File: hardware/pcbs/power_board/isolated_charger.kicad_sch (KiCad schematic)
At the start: 12 parts

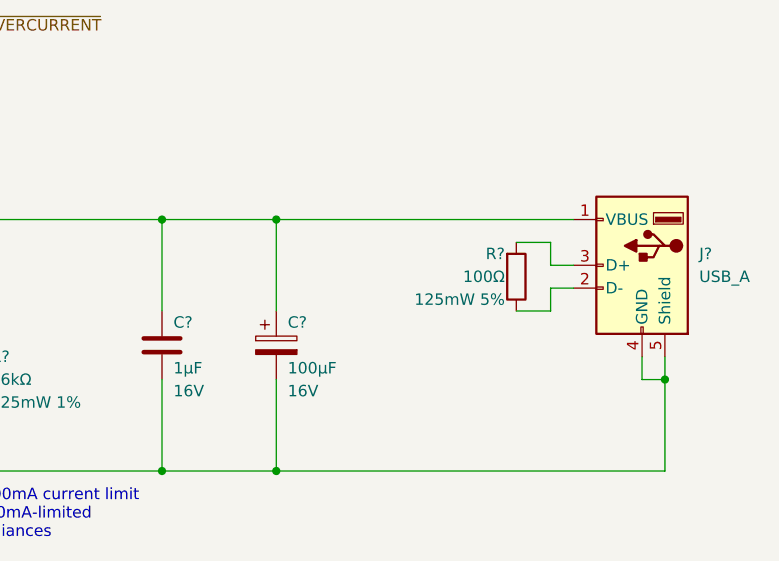
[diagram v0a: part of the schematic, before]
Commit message: power_board: schematic for fan controller
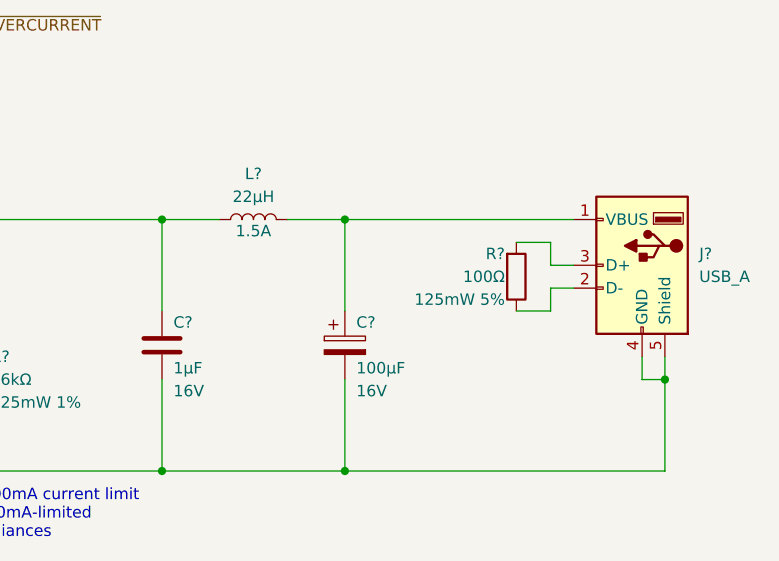
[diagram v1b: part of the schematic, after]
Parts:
- added L?: 22μH, Inductor_SMD:L_Sunlord_SWPA6045S, symbol Device:L
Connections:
- net at C?.1, U?.6 (OUT): now also L?.1; no longer C?.1, J?.1 (VBUS)
- new net: C?.1, J?.1 (VBUS), L?.2
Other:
- moved on the sheet: C?
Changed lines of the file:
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@@
   (junction (at 201.93 88.9) (diameter 0) (color 0 0 0 0)
   )
-  (junction (at 214.63 116.84) (diameter 0) (color 0 0 0 0)
-  )
   (junction (at 132.08 88.9) (diameter 0) (color 0 0 0 0)
   )
+  (junction (at 222.25 88.9) (diameter 0) (color 0 0 0 0)
+  )
   (junction (at 201.93 116.84) (diameter 0) (color 0 0 0 0)
   )
@@
   (junction (at 257.81 106.68) (diameter 0) (color 0 0 0 0)
   )
+  (junction (at 222.25 116.84) (diameter 0) (color 0 0 0 0)
+  )
   (junction (at 167.64 116.84) (diameter 0) (color 0 0 0 0)
   )
-  (junction (at 214.63 88.9) (diameter 0) (color 0 0 0 0)
-  )
   (junction (at 67.31 88.9) (diameter 0) (color 0 0 0 0)
   )
@@
     (stroke (width 0) (type default))
   )
-  (wire (pts (xy 201.93 116.84) (xy 214.63 116.84))
+  (wire (pts (xy 201.93 116.84) (xy 222.25 116.84))
     (stroke (width 0) (type default))
   )
@@
     (stroke (width 0) (type default))
   )
-  (wire (pts (xy 201.93 88.9) (xy 214.63 88.9))
+  (wire (pts (xy 201.93 88.9) (xy 208.28 88.9))
     (stroke (width 0) (type default))
   )
@@
     (stroke (width 0) (type default))
   )
+  (wire (pts (xy 222.25 116.84) (xy 257.81 116.84))
+    (stroke (width 0) (type default))
+  )
   (wire (pts (xy 138.43 52.07) (xy 152.4 52.07))
     (stroke (width 0) (type default))
@@
     (stroke (width 0) (type default))
   )
-  (wire (pts (xy 214.63 116.84) (xy 257.81 116.84))
-    (stroke (width 0) (type default))
-  )
   (wire (pts (xy 171.45 67.31) (xy 180.34 67.31))
     (stroke (width 0) (type default))
@@
     (stroke (width 0) (type default))
   )
-  (wire (pts (xy 214.63 88.9) (xy 247.65 88.9))
-    (stroke (width 0) (type default))
-  )
   (wire (pts (xy 132.08 88.9) (xy 132.08 99.06))
     (stroke (width 0) (type default))
@@
     (stroke (width 0) (type default))
   )
-  (wire (pts (xy 214.63 88.9) (xy 214.63 99.06))
+  (wire (pts (xy 222.25 88.9) (xy 222.25 99.06))
     (stroke (width 0) (type default))
   )
@@
     (stroke (width 0) (type default))
   )
+  (wire (pts (xy 222.25 88.9) (xy 247.65 88.9))
+    (stroke (width 0) (type default))
+  )
   (wire (pts (xy 132.08 88.9) (xy 138.43 88.9))
     (stroke (width 0) (type default))
@@
     (stroke (width 0) (type default))
   )
-  (wire (pts (xy 214.63 106.68) (xy 214.63 116.84))
+  (wire (pts (xy 222.25 106.68) (xy 222.25 116.84))
     (stroke (width 0) (type default))
   )
@@
   )
   (wire (pts (xy 152.4 62.23) (xy 152.4 67.31))
+    (stroke (width 0) (type default))
+  )
+  (wire (pts (xy 215.9 88.9) (xy 222.25 88.9))
     (stroke (width 0) (type default))
   )
@@
         (path "/4b166175-80a4-48c6-994d-6e62a6160b87/2e2b9578-5dbd-4b2d-88fb-256ac9c8dd75/bdb69c9c-123a-4faa-b5c1-7130aac5ebc2"
           (reference "C?") (unit 1)
+        )
+      )
+    )
+  )
+  (symbol (lib_id "Device:L") (at 212.09 88.9 90) (unit 1)
+    (in_bom yes) (on_board yes) (dnp no)
+    (property "Reference" "L?" (at 212.09 83.82 90)
+      (effects (font (size 1.27 1.27)))
+    )
+    (property "Value" "22μH" (at 212.09 86.36 90)
+      (effects (font (size 1.27 1.27)))
+    )
+    (property "Footprint" "Inductor_SMD:L_Sunlord_SWPA6045S" (at 212.09 88.9 0)
+      (effects (font (size 1.27 1.27)) hide)
+    )
+    (property "Datasheet" "~" (at 212.09 88.9 0)
+      (effects (font (size 1.27 1.27)) hide)
+    )
+    (property "Shop" "https://store.comet.bg/Catalogue/Product/49991/" (at 212.09 88.9 90)
+      (effects (font (size 1.27 1.27)) hide)
+    )
+    (property "Info" "1.5A" (at 212.09 90.17 90)
+      (effects (font (size 1.27 1.27)))
+    )
+    (pin "1")
+    (pin "2")
+    (instances
+      (project "power_board"
+        (path "/4b166175-80a4-48c6-994d-6e62a6160b87/2e2b9578-5dbd-4b2d-88fb-256ac9c8dd75/32f9baea-32bc-4a84-b83a-18c67cc6248e"
+          (reference "L?") (unit 1)
+        )
+        (path "/4b166175-80a4-48c6-994d-6e62a6160b87/2e2b9578-5dbd-4b2d-88fb-256ac9c8dd75/5f362cd5-d351-4250-994a-9f336837035c"
+          (reference "L?") (unit 1)
+        )
+        (path "/4b166175-80a4-48c6-994d-6e62a6160b87/2e2b9578-5dbd-4b2d-88fb-256ac9c8dd75/6373063e-1125-40d9-b0ec-3e2cb2886aea"
+          (reference "L?") (unit 1)
+        )
+        (path "/4b166175-80a4-48c6-994d-6e62a6160b87/2e2b9578-5dbd-4b2d-88fb-256ac9c8dd75/bdb69c9c-123a-4faa-b5c1-7130aac5ebc2"
+          (reference "L?") (unit 1)
         )
       )
@@
     )
   )
-  (symbol (lib_id "Device:C_Polarized") (at 214.63 102.87 0) (unit 1)
+  (symbol (lib_id "Device:C_Polarized") (at 222.25 102.87 0) (unit 1)
     (in_bom yes) (on_board yes) (dnp no)
-    (property "Reference" "C?" (at 215.9 100.33 0)
-      (effects (font (size 1.27 1.27)) (justify left))
-    )
-    (property "Value" "100μF" (at 215.9 105.41 0)
-      (effects (font (size 1.27 1.27)) (justify left))
-    )
-    (property "Footprint" "Capacitor_SMD:CP_Elec_6.3x5.4" (at 215.5952 106.68 0)
-      (effects (font (size 1.27 1.27)) hide)
-    )
-    (property "Datasheet" "~" (at 214.63 102.87 0)
-      (effects (font (size 1.27 1.27)) hide)
-    )
-    (property "Shop" "https://store.comet.bg/Catalogue/Product/29563/" (at 214.63 102.87 0)
-      (effects (font (size 1.27 1.27)) hide)
-    )
-    (property "Info" "16V" (at 215.9 107.95 0)
-      (effects (font (size 1.27 1.27)) (justify left))
-    )
+    (property "Reference" "C?" (at 223.52 100.33 0)
+      (effects (font (size 1.27 1.27)) (justify left))
+    )
+    (property "Value" "100μF" (at 223.52 105.41 0)
+      (effects (font (size 1.27 1.27)) (justify left))
+    )
+    (property "Footprint" "Capacitor_SMD:CP_Elec_6.3x5.4" (at 223.2152 106.68 0)
+      (effects (font (size 1.27 1.27)) hide)
+    )
+    (property "Datasheet" "~" (at 222.25 102.87 0)
+      (effects (font (size 1.27 1.27)) hide)
+    )
+    (property "Shop" "https://store.comet.bg/Catalogue/Product/29563/" (at 222.25 102.87 0)
+      (effects (font (size 1.27 1.27)) hide)
+    )
+    (property "Info" "16V" (at 223.52 107.95 0)
+      (effects (font (size 1.27 1.27)) (justify left))
+    )

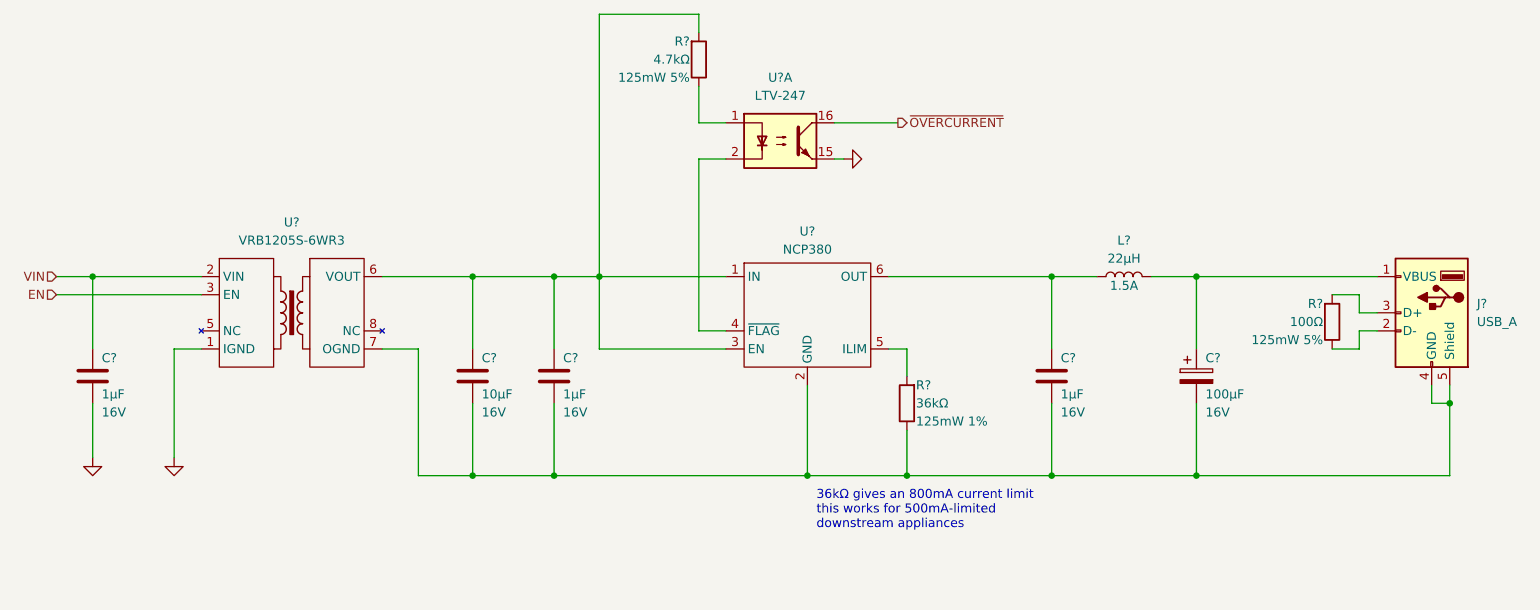
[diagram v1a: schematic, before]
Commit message: power_board: add temperature sensor and GPIOs to schematic
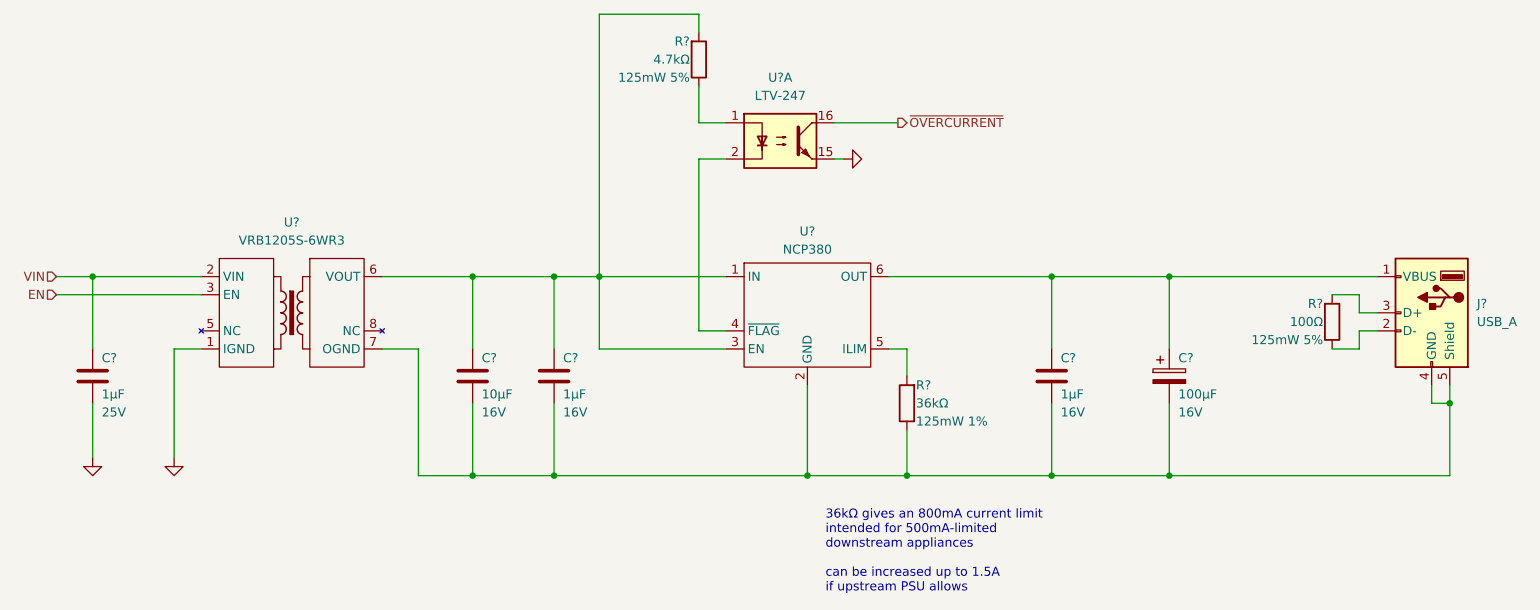
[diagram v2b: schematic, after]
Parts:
- removed L?: 22μH, Inductor_SMD:L_Sunlord_SWPA6045S, symbol Device:L
- C?: Info 16V -> 25V; Shop https://store.comet.bg/Catalogue/Product/16789/ -> https://store.comet.bg/Catalogue/Product/9031/
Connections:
- net at C?.1, U?.6 (OUT): now also C?.1, J?.1 (VBUS)
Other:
- note added: "36kΩ gives an 800mA current limit intended for 500mA-limited downstream appliances can be increased up to 1.5A if upstream PSU allows"
- note removed: "36kΩ gives an 800mA current limit this works for 500mA-limited downstream appliances"
- moved on the sheet: C?
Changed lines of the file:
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@@
   (junction (at 132.08 88.9) (diameter 0) (color 0 0 0 0)
   )
-  (junction (at 222.25 88.9) (diameter 0) (color 0 0 0 0)
-  )
   (junction (at 201.93 116.84) (diameter 0) (color 0 0 0 0)
   )
@@
   (junction (at 257.81 106.68) (diameter 0) (color 0 0 0 0)
   )
-  (junction (at 222.25 116.84) (diameter 0) (color 0 0 0 0)
+  (junction (at 218.44 116.84) (diameter 0) (color 0 0 0 0)
   )
   (junction (at 167.64 116.84) (diameter 0) (color 0 0 0 0)
@@
   (junction (at 67.31 88.9) (diameter 0) (color 0 0 0 0)
   )
+  (junction (at 218.44 88.9) (diameter 0) (color 0 0 0 0)
+  )
   (junction (at 181.61 116.84) (diameter 0) (color 0 0 0 0)
   )
@@
     (stroke (width 0) (type default))
   )
-  (wire (pts (xy 201.93 116.84) (xy 222.25 116.84))
+  (wire (pts (xy 201.93 116.84) (xy 218.44 116.84))
     (stroke (width 0) (type default))
   )
@@
     (stroke (width 0) (type default))
   )
-  (wire (pts (xy 201.93 88.9) (xy 208.28 88.9))
+  (wire (pts (xy 201.93 88.9) (xy 218.44 88.9))
     (stroke (width 0) (type default))
   )
@@
     (stroke (width 0) (type default))
   )
-  (wire (pts (xy 222.25 116.84) (xy 257.81 116.84))
-    (stroke (width 0) (type default))
-  )
   (wire (pts (xy 138.43 52.07) (xy 152.4 52.07))
     (stroke (width 0) (type default))
@@
     (stroke (width 0) (type default))
   )
-  (wire (pts (xy 222.25 88.9) (xy 222.25 99.06))
+  (wire (pts (xy 218.44 88.9) (xy 218.44 99.06))
     (stroke (width 0) (type default))
   )
@@
     (stroke (width 0) (type default))
   )
-  (wire (pts (xy 222.25 88.9) (xy 247.65 88.9))
+  (wire (pts (xy 218.44 88.9) (xy 247.65 88.9))
     (stroke (width 0) (type default))
   )
@@
     (stroke (width 0) (type default))
   )
+  (wire (pts (xy 218.44 116.84) (xy 257.81 116.84))
+    (stroke (width 0) (type default))
+  )
   (wire (pts (xy 67.31 106.68) (xy 67.31 114.3))
     (stroke (width 0) (type default))
@@
     (stroke (width 0) (type default))
   )
-  (wire (pts (xy 222.25 106.68) (xy 222.25 116.84))
+  (wire (pts (xy 218.44 106.68) (xy 218.44 116.84))
     (stroke (width 0) (type default))
   )
@@
     (stroke (width 0) (type default))
   )
-  (wire (pts (xy 215.9 88.9) (xy 222.25 88.9))
-    (stroke (width 0) (type default))
-  )
   (wire (pts (xy 152.4 96.52) (xy 152.4 72.39))
     (stroke (width 0) (type default))
@@
     (stroke (width 0) (type default))
   )
-  (text "36kΩ gives an 800mA current limit\nthis works for 500mA-limited\ndownstream appliances"
-    (at 168.91 124.46 0)
+  (text "36kΩ gives an 800mA current limit\nintended for 500mA-limited\ndownstream appliances\n\ncan be increased up to 1.5A\nif upstream PSU allows"
+    (at 170.18 133.35 0)
     (effects (font (size 1.27 1.27)) (justify left bottom))
   )
@@
       (effects (font (size 1.27 1.27)) hide)
     )
-    (property "Info" "16V" (at 68.58 107.95 0)
-      (effects (font (size 1.27 1.27)) (justify left))
-    )
-    (property "Shop" "https://store.comet.bg/Catalogue/Product/16789/" (at 67.31 102.87 0)
+    (property "Info" "25V" (at 68.58 107.95 0)
+      (effects (font (size 1.27 1.27)) (justify left))
+    )
+    (property "Shop" "https://store.comet.bg/Catalogue/Product/9031/" (at 67.31 102.87 0)
       (effects (font (size 1.27 1.27)) hide)
     )
@@
         (path "/4b166175-80a4-48c6-994d-6e62a6160b87/2e2b9578-5dbd-4b2d-88fb-256ac9c8dd75/bdb69c9c-123a-4faa-b5c1-7130aac5ebc2"
           (reference "C?") (unit 1)
-        )
-      )
-    )
-  )
-  (symbol (lib_id "Device:L") (at 212.09 88.9 90) (unit 1)
-    (in_bom yes) (on_board yes) (dnp no)
-    (property "Reference" "L?" (at 212.09 83.82 90)
-      (effects (font (size 1.27 1.27)))
-    )
-    (property "Value" "22μH" (at 212.09 86.36 90)
-      (effects (font (size 1.27 1.27)))
-    )
-    (property "Footprint" "Inductor_SMD:L_Sunlord_SWPA6045S" (at 212.09 88.9 0)
-      (effects (font (size 1.27 1.27)) hide)
-    )
-    (property "Datasheet" "~" (at 212.09 88.9 0)
-      (effects (font (size 1.27 1.27)) hide)
-    )
-    (property "Shop" "https://store.comet.bg/Catalogue/Product/49991/" (at 212.09 88.9 90)
-      (effects (font (size 1.27 1.27)) hide)
-    )
-    (property "Info" "1.5A" (at 212.09 90.17 90)
-      (effects (font (size 1.27 1.27)))
-    )
-    (pin "1")
-    (pin "2")
-    (instances
-      (project "power_board"
-        (path "/4b166175-80a4-48c6-994d-6e62a6160b87/2e2b9578-5dbd-4b2d-88fb-256ac9c8dd75/32f9baea-32bc-4a84-b83a-18c67cc6248e"
-          (reference "L?") (unit 1)
-        )
-        (path "/4b166175-80a4-48c6-994d-6e62a6160b87/2e2b9578-5dbd-4b2d-88fb-256ac9c8dd75/5f362cd5-d351-4250-994a-9f336837035c"
-          (reference "L?") (unit 1)
-        )
-        (path "/4b166175-80a4-48c6-994d-6e62a6160b87/2e2b9578-5dbd-4b2d-88fb-256ac9c8dd75/6373063e-1125-40d9-b0ec-3e2cb2886aea"
-          (reference "L?") (unit 1)
-        )
-        (path "/4b166175-80a4-48c6-994d-6e62a6160b87/2e2b9578-5dbd-4b2d-88fb-256ac9c8dd75/bdb69c9c-123a-4faa-b5c1-7130aac5ebc2"
-          (reference "L?") (unit 1)
         )
       )
@@
     )
   )
-  (symbol (lib_id "Device:C_Polarized") (at 222.25 102.87 0) (unit 1)
+  (symbol (lib_id "Device:C_Polarized") (at 218.44 102.87 0) (unit 1)
     (in_bom yes) (on_board yes) (dnp no)
-    (property "Reference" "C?" (at 223.52 100.33 0)
-      (effects (font (size 1.27 1.27)) (justify left))
-    )
-    (property "Value" "100μF" (at 223.52 105.41 0)
-      (effects (font (size 1.27 1.27)) (justify left))
-    )
-    (property "Footprint" "Capacitor_SMD:CP_Elec_6.3x5.4" (at 223.2152 106.68 0)
-      (effects (font (size 1.27 1.27)) hide)
-    )
-    (property "Datasheet" "~" (at 222.25 102.87 0)
-      (effects (font (size 1.27 1.27)) hide)
-    )
-    (property "Shop" "https://store.comet.bg/Catalogue/Product/29563/" (at 222.25 102.87 0)
-      (effects (font (size 1.27 1.27)) hide)
-    )
-    (property "Info" "16V" (at 223.52 107.95 0)
-      (effects (font (size 1.27 1.27)) (justify left))
-    )
+    (property "Reference" "C?" (at 219.71 100.33 0)
+      (effects (font (size 1.27 1.27)) (justify left))
+    )
+    (property "Value" "100μF" (at 219.71 105.41 0)
+      (effects (font (size 1.27 1.27)) (justify left))
+    )
+    (property "Footprint" "Capacitor_SMD:CP_Elec_6.3x5.4" (at 219.4052 106.68 0)
+      (effects (font (size 1.27 1.27)) hide)
+    )
+    (property "Datasheet" "~" (at 218.44 102.87 0)
+      (effects (font (size 1.27 1.27)) hide)
+    )
+    (property "Shop" "https://store.comet.bg/Catalogue/Product/29563/" (at 218.44 102.87 0)
+      (effects (font (size 1.27 1.27)) hide)
+    )
+    (property "Info" "16V" (at 219.71 107.95 0)
+      (effects (font (size 1.27 1.27)) (justify left))
+    )

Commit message: power_board: minor fixes to shematic
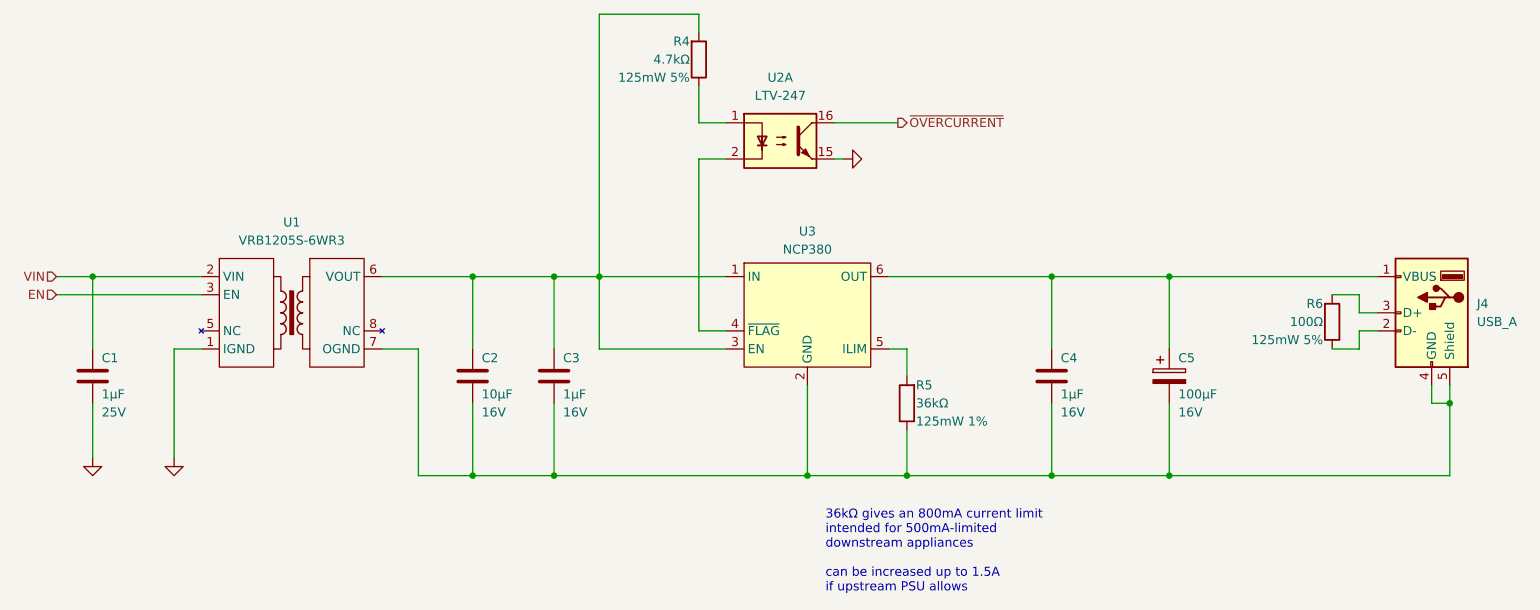
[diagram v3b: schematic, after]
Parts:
- gave numbers to parts that had none: 12

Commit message: power_board: finalise all footprints
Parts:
- J4: footprint (none) -> conn:USB_A_Amphenol_UE27AC5410H
- U2: Shop (none) -> https://eu.mouser.com/ProductDetail/Lite-On/LTV-247?qs=9ayh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
- U3: Shop (none) -> https://eu.mouser.com/ProductDetail/onsemi/NCP380LSNAJAAT1G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
- renumbered C1 to C2, C2 to C3, C3 to C4, C4 to C5, C5 to C6
